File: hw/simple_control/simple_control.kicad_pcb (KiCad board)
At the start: 4 copper layers, 99.1 x 99.1 mm, 87 parts, among them J101 Screw_Terminal_01x02, J102 Jack-DC, J103 Screw_Terminal_01x03, J104 Screw_Terminal_01x03, J1301 Micro_SD_Card, J1401 Conn_02x05_Odd_Even, J601 Conn_01x04, J602 Raspberry_Pi_0_2_3, J603 Conn_01x03, Q1001 BC817, Q201 AOSP21357, Q701 BC817, Q801 BC817, Q901 BC817, SW1201 SW_Push, SW601 SW_Push, U1101 CAT24C256, U301 SN74AHCT125D, U601 PicoW

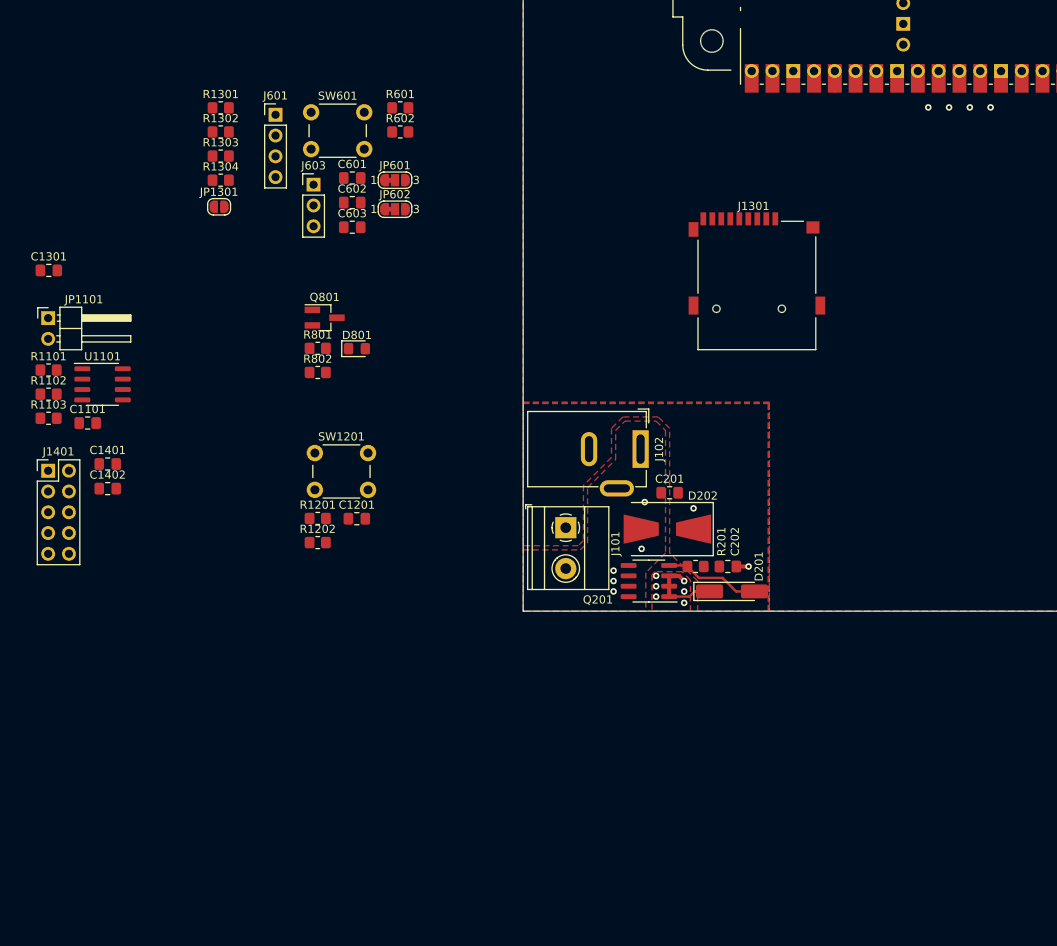
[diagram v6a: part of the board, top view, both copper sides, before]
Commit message: chore(hw): add more buttons
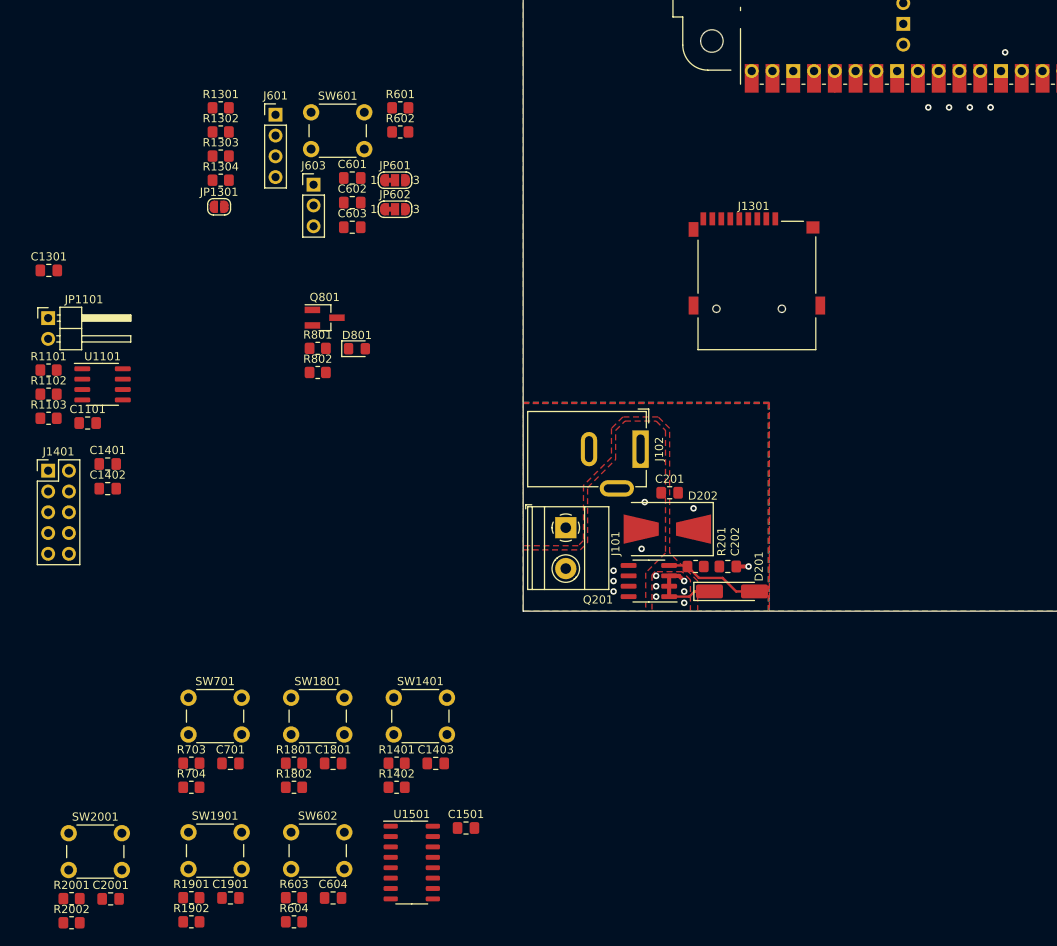
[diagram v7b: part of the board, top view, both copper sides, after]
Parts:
- removed C1201: 100n, Capacitor_SMD:C_0805_2012Metric_Pad1.18x1.45mm_HandSolder
- removed R1201: 100K, Resistor_SMD:R_0805_2012Metric_Pad1.20x1.40mm_HandSolder
- removed R1202: 10K, Resistor_SMD:R_0805_2012Metric_Pad1.20x1.40mm_HandSolder
- removed SW1201: SW_Push, Button_Switch_THT:SW_PUSH_6mm
- added C1403: 100n, Capacitor_SMD:C_0805_2012Metric_Pad1.18x1.45mm_HandSolder, F.Cu at (90.9, 158.3)
- added C1501: 100n, Capacitor_SMD:C_0805_2012Metric_Pad1.18x1.45mm_HandSolder, F.Cu at (94.6, 166.2)
- added C1801: 100n, Capacitor_SMD:C_0805_2012Metric_Pad1.18x1.45mm_HandSolder, F.Cu at (78.4, 158.3)
- added C1901: 100n, Capacitor_SMD:C_0805_2012Metric_Pad1.18x1.45mm_HandSolder, F.Cu at (65.8, 174.8)
- added C2001: 100n, Capacitor_SMD:C_0805_2012Metric_Pad1.18x1.45mm_HandSolder, F.Cu at (51.2, 174.9)
- added C604: 100n, Capacitor_SMD:C_0805_2012Metric_Pad1.18x1.45mm_HandSolder, F.Cu at (78.4, 174.8)
- added C701: 100n, Capacitor_SMD:C_0805_2012Metric_Pad1.18x1.45mm_HandSolder, F.Cu at (65.8, 158.3)
- added R1401: 100K, Resistor_SMD:R_0805_2012Metric_Pad1.20x1.40mm_HandSolder, F.Cu at (86.1, 158.3)
- added R1402: 10K, Resistor_SMD:R_0805_2012Metric_Pad1.20x1.40mm_HandSolder, F.Cu at (86.1, 161.2)
- added R1801: 100K, Resistor_SMD:R_0805_2012Metric_Pad1.20x1.40mm_HandSolder, F.Cu at (73.6, 158.3)
- added R1802: 10K, Resistor_SMD:R_0805_2012Metric_Pad1.20x1.40mm_HandSolder, F.Cu at (73.6, 161.2)
- added R1901: 100K, Resistor_SMD:R_0805_2012Metric_Pad1.20x1.40mm_HandSolder, F.Cu at (61.0, 174.7)
- added R1902: 10K, Resistor_SMD:R_0805_2012Metric_Pad1.20x1.40mm_HandSolder, F.Cu at (61.0, 177.7)
- added R2001: 100K, Resistor_SMD:R_0805_2012Metric_Pad1.20x1.40mm_HandSolder, F.Cu at (46.4, 174.8)
- added R2002: 10K, Resistor_SMD:R_0805_2012Metric_Pad1.20x1.40mm_HandSolder, F.Cu at (46.4, 177.8)
- added R603: 100K, Resistor_SMD:R_0805_2012Metric_Pad1.20x1.40mm_HandSolder, F.Cu at (73.6, 174.7)
- added R604: 10K, Resistor_SMD:R_0805_2012Metric_Pad1.20x1.40mm_HandSolder, F.Cu at (73.6, 177.7)
- added R703: 100K, Resistor_SMD:R_0805_2012Metric_Pad1.20x1.40mm_HandSolder, F.Cu at (61.0, 158.3)
- added R704: 10K, Resistor_SMD:R_0805_2012Metric_Pad1.20x1.40mm_HandSolder, F.Cu at (61.0, 161.2)
- added SW1401: SW_Push, Button_Switch_THT:SW_PUSH_6mm, F.Cu at (85.8, 150.3)
- added SW1801: SW_Push, Button_Switch_THT:SW_PUSH_6mm, F.Cu at (73.2, 150.3)
- added SW1901: SW_Push, Button_Switch_THT:SW_PUSH_6mm, F.Cu at (60.7, 166.7)
- added SW2001: SW_Push, Button_Switch_THT:SW_PUSH_6mm, F.Cu at (46.0, 166.8)
- added SW602: SW_Push, Button_Switch_THT:SW_PUSH_6mm, F.Cu at (73.2, 166.7)
- added SW701: SW_Push, Button_Switch_THT:SW_PUSH_6mm, F.Cu at (60.7, 150.3)
- added U1501: 4050, Package_SO:SO-16_3.9x9.9mm_P1.27mm, F.Cu at (88.0, 170.4)
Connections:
- J602 pad 12: unconnected-(J602-GPIO18/PWM0-Pad12) -> /CPU/BUTTON4
- J602 pad 26: unconnected-(J602-~{CE1}/GPIO7-Pad26) -> /CPU/BUTTON5
- U601 pad 31: unconnected-(U601-GPIO26_ADC0-Pad31) -> /CPU/BUTTON5
- U601 pad 32: unconnected-(U601-GPIO27_ADC1-Pad32) -> /CPU/BUTTON4
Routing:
- net /CPU/BUTTON4: track 0.00 -> 36.2 mm, vias 0 -> 1

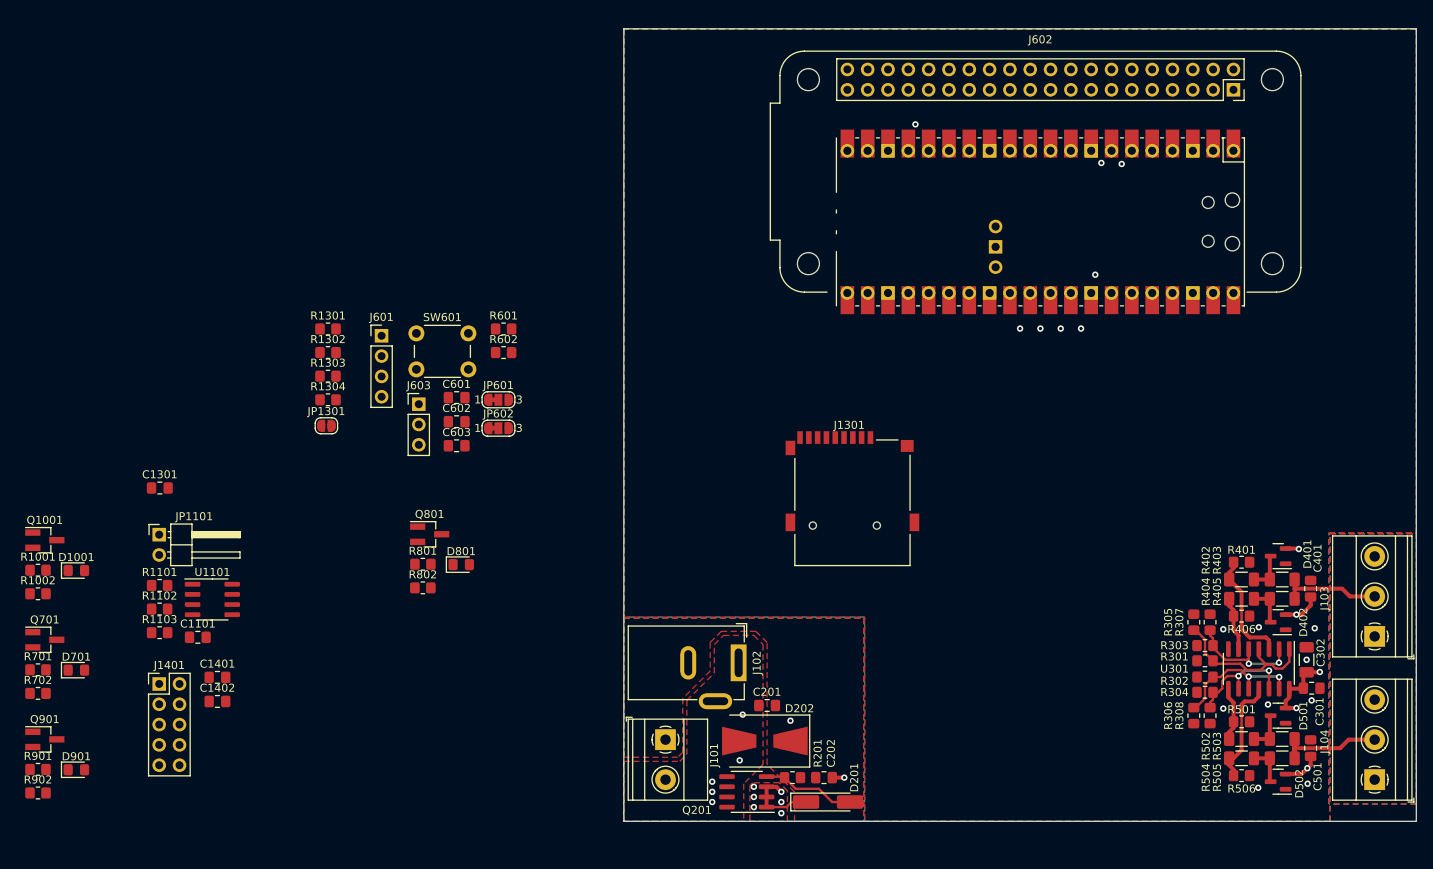
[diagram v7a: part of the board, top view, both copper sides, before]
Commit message: chore(hw): move blocks around
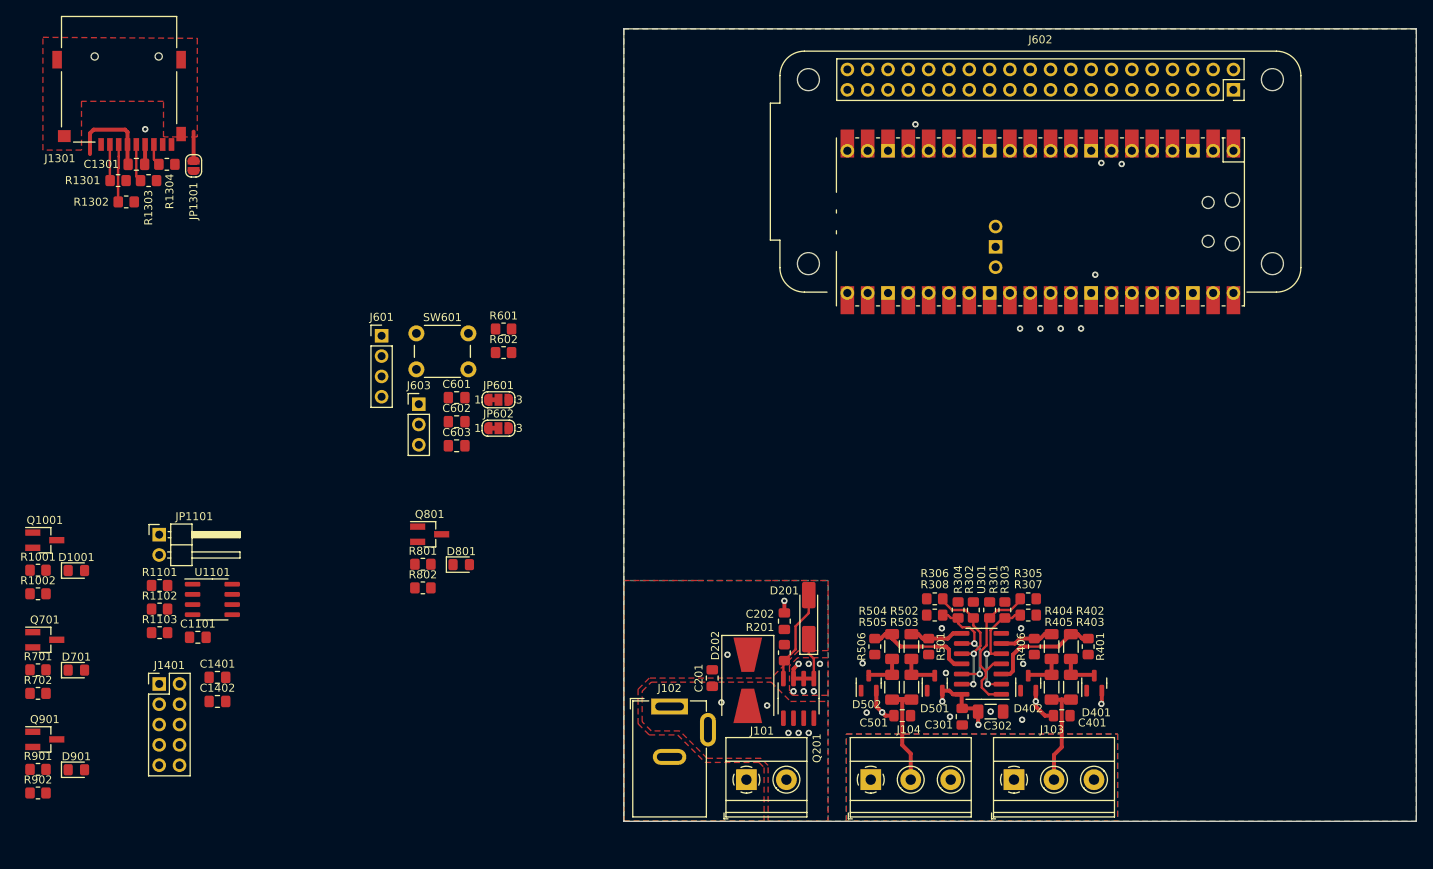
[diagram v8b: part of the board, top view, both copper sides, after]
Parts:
- moved J1301 108.8 mm to (38.5, 44.1), turned to 180 degrees
- moved J104 63.0 mm to (132.5, 134.5), turned to 0 degrees
- moved D502 52.6 mm to (132.2, 122.4), turned to 90 degrees
- moved C501 51.2 mm to (136.4, 126.5), turned to 0 degrees
- moved R505 49.6 mm to (135.1, 122.9), turned to 90 degrees
- moved R506 48.6 mm to (133.0, 117.9), turned to -90 degrees
- moved J103 48.5 mm to (150.4, 134.5), turned to 0 degrees
- moved R503 46.8 mm to (137.5, 122.9), turned to 90 degrees
- moved R504 45.9 mm to (135.1, 117.9), turned to 90 degrees
- moved C301 43.8 mm to (143.9, 126.6), turned to -90 degrees
- moved D501 43.1 mm to (140.5, 122.4), turned to 90 degrees
- moved R502 42.9 mm to (137.5, 117.9), turned to 90 degrees
- moved C1301 40.6 mm to (40.7, 57.6), turned to 180 degrees
- moved R501 40.2 mm to (139.7, 117.9), turned to 90 degrees
- moved C302 40.0 mm to (147.4, 126.0), turned to 0 degrees
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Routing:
- net +3.3V: track 24.1 -> 35.8 mm
- net Net-(J1301-CMD): track 0.00 -> 7.22 mm
- net Net-(J1301-CLK): track 0.00 -> 4.74 mm
- net Net-(J1301-DAT3/CD): track 0.00 -> 4.52 mm
- net Net-(J1301-SHIELD): track 0.00 -> 3.62 mm
- net Net-(J1301-DAT0): track 0.00 -> 2.74 mm
- net GND: track 0.00 -> 2.50 mm, vias 10 -> 11
- added copper zone on F.Cu, net Net-(J1301-SHIELD)
